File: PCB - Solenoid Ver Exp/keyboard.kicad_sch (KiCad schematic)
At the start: 180 parts, among them J1 HRO_TYPE-C-31-M-12, J2 Conn_01x03, Q1 AO3400A, Q2 AO3400A, Q3 AO3400A, Q4 AO3400A, Q5 AO3400A, Q6 AO3400A, SW1 Alps SKRK, SW2 Alps SKRK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

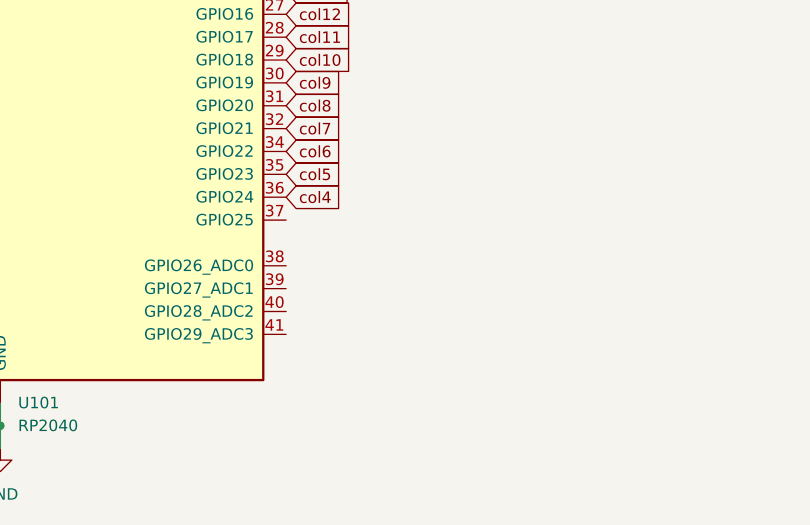
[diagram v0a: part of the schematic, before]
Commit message: general improvements in reliability + added 5 spare gpio headder
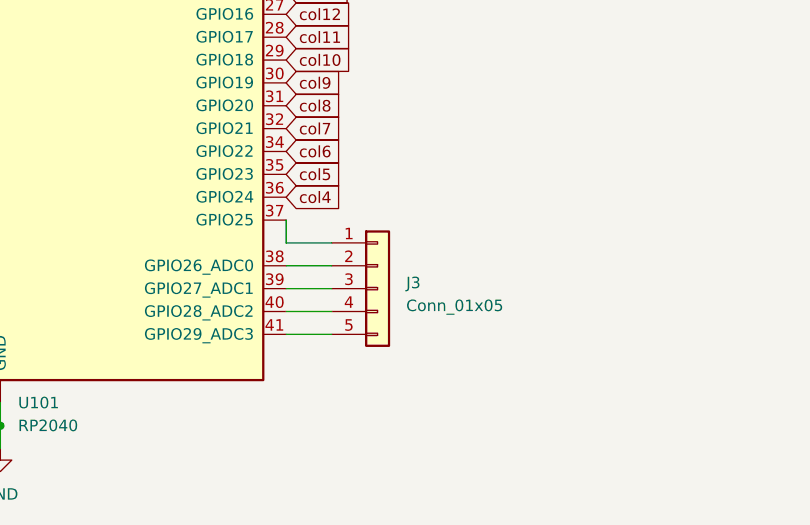
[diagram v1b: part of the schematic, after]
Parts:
- added J3: Conn_01x05, Connector_PinHeader_2.54mm:PinHeader_1x05_P2.54mm_Vertical, symbol Connector_Generic:Conn_01x05
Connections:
- net at U101.37 (GPIO25): now also J3.1 (Pin_1)
- net at U101.38 (GPIO26_ADC0): now also J3.2 (Pin_2)
- net at U101.39 (GPIO27_ADC1): now also J3.3 (Pin_3)
- net at U101.40 (GPIO28_ADC2): now also J3.4 (Pin_4)
- net at U101.41 (GPIO29_ADC3): now also J3.5 (Pin_5)
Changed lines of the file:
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@@
+    (stroke (width 0) (type default))
+  )
+  (wire (pts (xy 287.02 265.43) (xy 281.94 265.43))
     (stroke (width 0) (type default))
   )
@@
     (stroke (width 0) (type default))
   )
+  (wire (pts (xy 281.94 255.27) (xy 281.94 252.73))
+    (stroke (width 0) (type default))
+  )
   (wire (pts (xy 161.29 86.36) (xy 186.69 86.36))
     (stroke (width 0) (type default))
@@
     (stroke (width 0) (type default))
   )
+  (wire (pts (xy 287.02 260.35) (xy 281.94 260.35))
+    (stroke (width 0) (type default))
+  )
   (wire (pts (xy 110.49 86.36) (xy 135.89 86.36))
     (stroke (width 0) (type default))
@@
     (stroke (width 0) (type default))
   )
+  (wire (pts (xy 287.02 255.27) (xy 281.94 255.27))
+    (stroke (width 0) (type default))
+  )
   (wire (pts (xy 121.92 24.13) (xy 121.92 49.53))
     (stroke (width 0) (type default))
@@
     (stroke (width 0) (type default))
   )
+  (wire (pts (xy 287.02 257.81) (xy 281.94 257.81))
+    (stroke (width 0) (type default))
+  )
   (wire (pts (xy 135.89 111.76) (xy 161.29 111.76))
     (stroke (width 0) (type default))
@@
   )
   (wire (pts (xy 22.86 86.36) (xy 34.29 86.36))
+    (stroke (width 0) (type default))
+  )
+  (wire (pts (xy 287.02 262.89) (xy 281.94 262.89))
     (stroke (width 0) (type default))
   )
@@
         )
       )
+    )
+  )
+  (symbol (lib_id "Connector_Generic:Conn_01x05") (at 292.1 260.35 0) (unit 1)
+    (in_bom yes) (on_board yes) (dnp no) (fields_autoplaced)
+    (property "Reference" "J3" (at 295.275 259.715 0)
+      (effects (font (size 1.27 1.27)) (justify left))
+    )
+    (property "Value" "Conn_01x05" (at 295.275 262.255 0)
+      (effects (font (size 1.27 1.27)) (justify left))
+    )
+    (property "Footprint" "Connector_PinHeader_2.54mm:PinHeader_1x05_P2.54mm_Vertical" (at 292.1 260.35 0)
+      (effects (font (size 1.27 1.27)) hide)
+    )
+    (property "Datasheet" "~" (at 292.1 260.35 0)
+      (effects (font (size 1.27 1.27)) hide)
+    )
+    (pin "1")
+    (pin "2")
+    (pin "3")
+    (pin "4")
+    (pin "5")
+    (instances
+      (project "keyboard"
+        (path "/e2239ee3-9536-435b-859e-75484153df17"
+          (reference "J3") (unit 1)
+        )
+      )

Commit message: various updates and adjustments, created case for board will upload later
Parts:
- removed L1: SWPA4030S100MT, Inductor_SMD:L_Sunlord_SWPA4030S, symbol Device:L_Small
- added C13: 0.1uF 0402, Capacitor_SMD:C_0402_1005Metric, symbol Device:C_Small
- added C18: 100uF 0402, Capacitor_SMD:C_0402_1005Metric, symbol Device:C_Small
- added C19: 1uF 0402, Capacitor_SMD:C_0402_1005Metric, symbol Device:C_Small
- added R10, R9: 10K 0402, Resistor_SMD:R_0402_1005Metric, symbol Device:R_Small
- added R11: 17.4kΩ 0402, Resistor_SMD:R_0402_1005Metric, symbol Device:R_Small
- added U2: AP22615, Package_TO_SOT_SMD:TSOT-23-6, symbol AP22615:AP22615
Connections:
- net GND: now also C13.2, C18.2, C19.2, R11.2, U2.2 (GND)
- net VBUS: now also C19.1, R10.1, R9.1, U2.6 (IN); no longer D1.2 (A)
- net at C9.2, D2.1 (K), D3.1 (K)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: now also D1.1 (K)
- new net: R10.2, U2.3 (FLG)
- new net: R9.2, U2.4 (EN)
- new net: R11.1, U2.5 (ISET)
- new net VSYS: C13.1, C18.1, D1.2 (A), U2.1 (OUT)
